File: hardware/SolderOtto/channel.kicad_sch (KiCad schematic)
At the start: 16 parts, among them J601 Conn_01x07

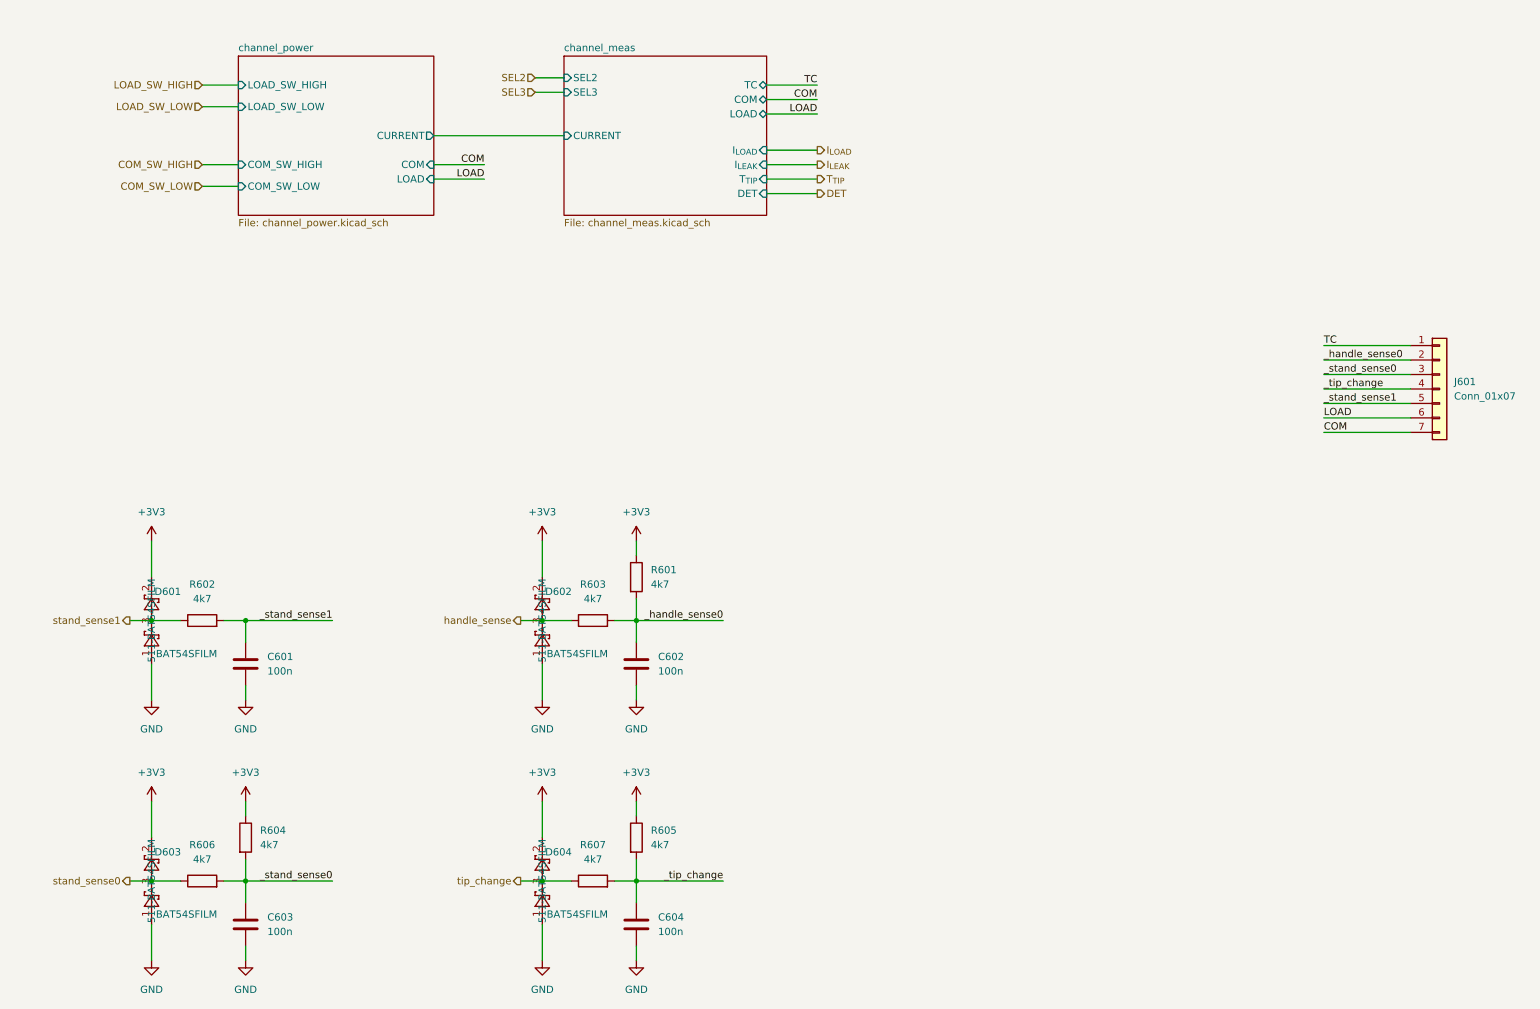
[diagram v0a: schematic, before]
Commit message: add support for tweezers AM-120
change mcu to stm32h573VI
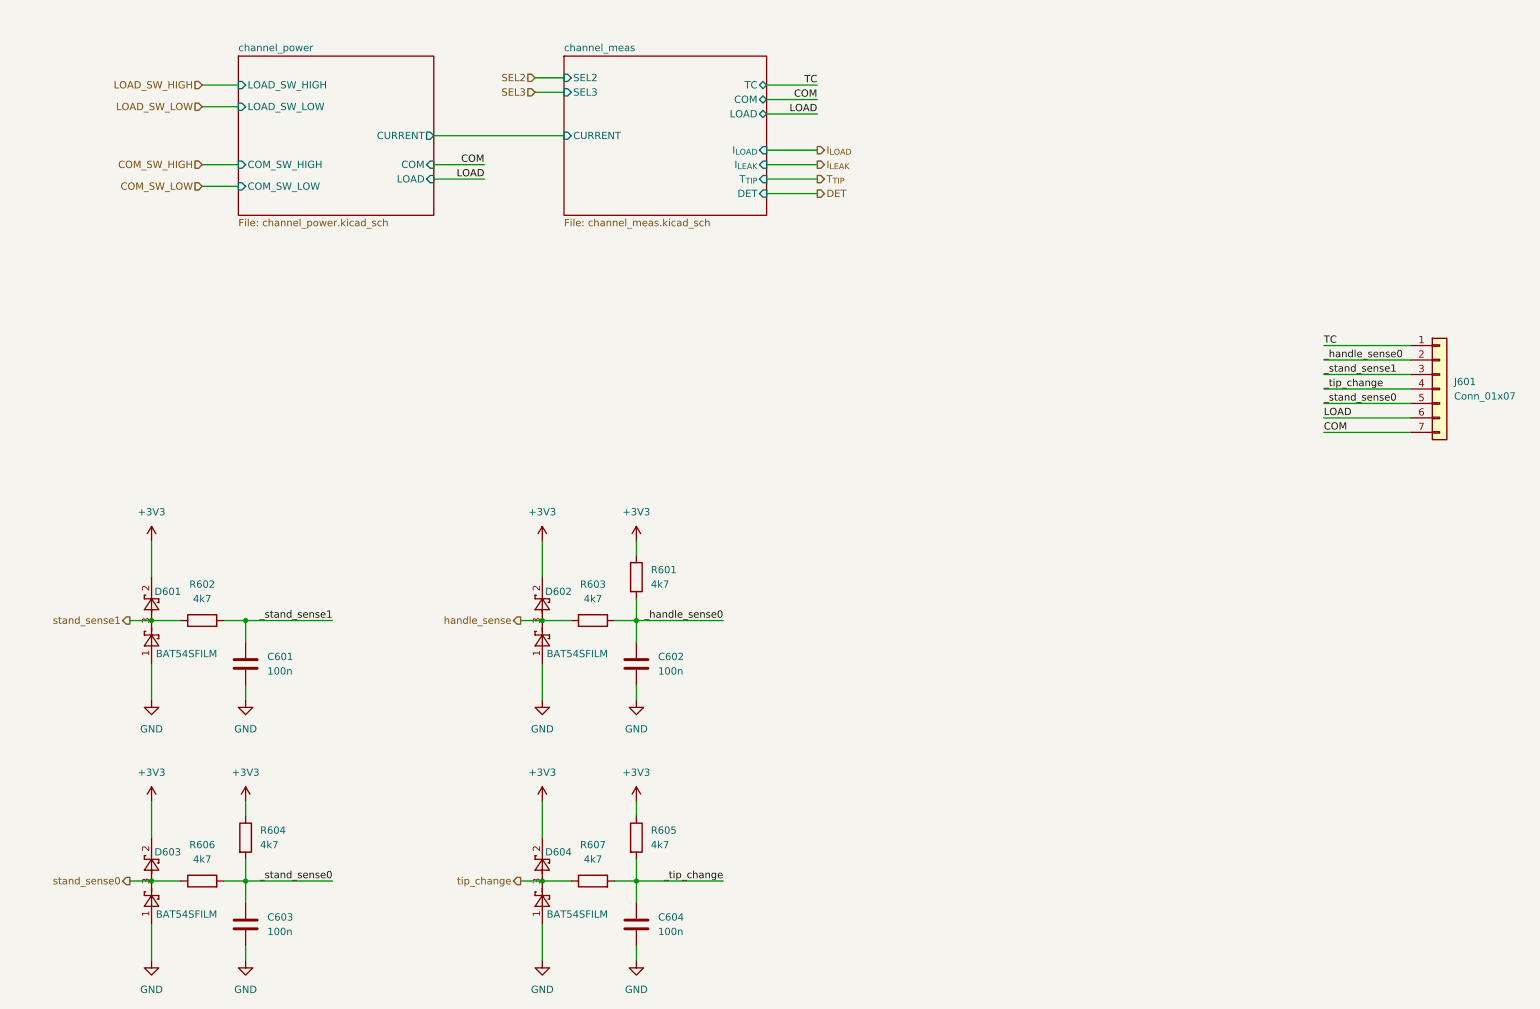
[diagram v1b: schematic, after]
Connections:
- net _stand_sense0: now also J601.5 (Pin_5); no longer J601.3 (Pin_3)
- net _stand_sense1: now also J601.3 (Pin_3); no longer J601.5 (Pin_5)
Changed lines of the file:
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@@
 	)
 	(label "_stand_sense0"
-		(at 248.92 86.36 0)
+		(at 248.92 91.44 0)
 		(fields_autoplaced yes)
 		(effects
@@
 	)
 	(label "_stand_sense1"
-		(at 248.92 91.44 0)
+		(at 248.92 86.36 0)
 		(fields_autoplaced yes)
 		(effects
@@
 	)
 	(symbol
+		(lib_name "BAT54SFILM_1")
 		(lib_id "mylib_diodes:BAT54SFILM")
 		(at 43.18 175.26 90)
@@
 					(size 1.27 1.27)
 				)
+				(hide yes)
 			)
 		)
@@
 					(size 1.27 1.27)
 				)
+				(hide yes)
 			)
 		)
@@
 					(size 1.27 1.27)
 				)
+				(hide yes)
 			)
 		)
@@
 					(size 1.27 1.27)
 				)
+				(hide yes)
 			)
 		)
@@
 			(project "SolderOtto"
 				(path "/04e99464-bf33-4a4f-8397-d26b5ec904f3/57a4c2b0-a7ab-4dc9-9bcc-6bd7e1b882d1"
-					(page "7")
+					(page "8")
 				)
 			)
@@
 			(project "SolderOtto"
 				(path "/04e99464-bf33-4a4f-8397-d26b5ec904f3/57a4c2b0-a7ab-4dc9-9bcc-6bd7e1b882d1"
-					(page "8")
-				)
-			)
+					(page "9")
+				)
+			)

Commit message: save wip
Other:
- added sheet power_latch (power_latch.kicad_sch)

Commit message: wip
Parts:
- added D605, D606: D, symbol Device:D
- added HEATER601: AM120, symbol mylib_connectors:JBC-AM120
- added HEATER602: T245, symbol mylib_connectors:JBC-T245
- added HEATER603: T210, symbol mylib_connectors:JBC-T210
- added X601, X603, X605: Binder_IP40_07, symbol mylib_connectors:Binder_IP40_07
- added X602: Binder_IP40_06, symbol mylib_connectors:Binder_IP40_06
- added X604, X606: Hirose RPC1-12RB-6P, symbol mylib_connectors:Hirose RPC1-12RB-6P
- D601: value BAT54SFILM -> BAS70S; Mouser 511-BAT54SFILM -> 3757-BAS70S_R1_00001CT-ND
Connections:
- net _handle_sense0 renamed _handle_id
- net _stand_sense0 renamed _stand_sense
- net _stand_sense1 renamed _iron_sense
- net handle_sense renamed handle_id
- net stand_sense0 renamed stand_sense
- net stand_sense1 renamed iron_sense
- new net: HEATER603.1, X605.1, X606.1
- new net: HEATER603.2, X605.6, X606.2
- new net: HEATER603.5, X605.7, X606.5
- new net: HEATER603.6, X605.2, X606.6
- new net: HEATER602.1, X603.1, X604.1
- new net: HEATER602.2, X603.6, X604.2
- new net: HEATER602.5, X603.7, X604.5
- new net: X603.2, X604.6
- new net: D605.1 (K), D606.2 (A), X601.7
- new net: D605.2 (A), HEATER601.4, X602.4
- new net: X605.3, X605.5
- new net: D606.1 (K), HEATER601.3, X602.3
- new net: HEATER601.1, X601.1, X602.1
- new net: HEATER601.2, X601.3, X602.2
- new net: HEATER601.5, X601.6, X602.5
- new net: HEATER601.6, X601.2, X602.6
- new net: X603.3, X603.5
- no-connect marks 0 -> 6
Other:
- sheet channel_meas ports: added LOAD0, LOAD1, SEL1; removed LOAD
- sheet channel_power ports: added LOAD0, LOAD0_SW_HIGH, LOAD1, LOAD1_SW_HIGH; removed LOAD, LOAD_SW_HIGH
- sheet power_latch ports: added COM_SW, IN_LOAD0_H, IN_LOAD1_H, OUT_LOAD0_H, OUT_LOAD1_H; removed IN_COM_L, IN_LOAD_H, IN_LOAD_L, OUT_LOAD_H
- note added: "AM-AD-SF"
- note added: "AM-SB"
- moved on the sheet: C601, C602, C603, C604, D601, D602, D603, D604, J601, R601, R602, R603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

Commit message: save wip
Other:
- sheet power_latch ports: added LOW_SIDE_SW; removed COM_SW

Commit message: update schematic
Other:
- sheet power_latch ports: added IN_COM, IN_LOAD0, IN_LOAD1, LOW_SIDE; removed IN_COM_H, IN_LOAD0_H, IN_LOAD1_H, LOW_SIDE_SW

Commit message: fix electrical findings
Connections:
- no-connect marks 6 -> 8
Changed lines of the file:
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@@
 	)
 	(no_connect
+		(at 35.56 87.63)
+	)
+	(no_connect
+		(at 38.1 83.82)
+	)
+	(no_connect
 		(at 58.42 121.92)
 	)
@@
 	)
 	(symbol
+		(lib_id "mylib_connectors:JBC-AM120")
+		(at 100.33 86.36 0)
+		(unit 1)
+		(exclude_from_sim yes)
+		(in_bom no)
+		(on_board no)
+		(dnp no)
+		(fields_autoplaced yes)
+		(property "Reference" "HEATER601"
+			(at 111.76 85.4074 0)
+			(effects
+				(font
+					(size 1.27 1.27)
+				)
+				(justify left)
+			)
+		)
+		(property "Value" "AM120"
+			(at 111.76 87.9474 0)
+			(effects
+				(font
+					(size 1.27 1.27)
+				)
+				(justify left)
+			)
+		)
+		(property "Footprint" ""
+			(at 49.53 87.63 0)
+			(effects
+				(font
+					(size 1.27 1.27)
+				)
+				(hide yes)
+			)
+		)
+		(property "Datasheet" ""
+			(at 49.53 87.63 0)
+			(effects
+				(font
+					(size 1.27 1.27)
+				)
+				(hide yes)
+			)
+		)
+		(property "Description" ""
+			(at 49.53 87.63 0)
+			(effects
+				(font
+					(size 1.27 1.27)
+				)
+				(hide yes)
+			)
+		)
+		(pin "2"
+		)
+		(pin "3"
+		)
+		(pin "4"
+		)
+		(pin "5"
+		)
+		(pin "1"
+		)
+		(pin "1"
+		)
+		(pin "6"
+		)
+		(instances
+			(project ""
+				(path "/04e99464-bf33-4a4f-8397-d26b5ec904f3/57a4c2b0-a7ab-4dc9-9bcc-6bd7e1b882d1"
+					(reference "HEATER601")
+					(unit 1)
+				)
+			)
+		)
+	)
+	(symbol
 		(lib_id "mylib_connectors:Hirose RPC1-12RB-6P")
 		(at 62.23 157.48 90)
@@
 					(unit 1)
 				)
-			)
-		)
-	)
-	(symbol
-		(lib_id "mylib_connectors:JBC-AM120")
-		(at 100.33 86.36 0)
-		(unit 1)
-		(exclude_from_sim yes)
-		(in_bom no)
-		(on_board no)
-		(dnp no)
-		(property "Reference" "HEATER601"
-			(at 111.76 85.4074 0)
-			(effects
-				(font
-					(size 1.27 1.27)
-				)
-				(justify left)
-				(hide yes)
-			)
-		)
-		(property "Value" "AM120"
-			(at 97.028 71.12 0)
-			(effects
-				(font
-					(size 1.27 1.27)
-				)
-				(justify left)
-			)
-		)
-		(property "Footprint" ""
-			(at 49.53 87.63 0)
-			(effects
-				(font
-					(size 1.27 1.27)
-				)
-				(hide yes)
-			)
-		)
-		(property "Datasheet" ""
-			(at 49.53 87.63 0)
-			(effects
-				(font
-					(size 1.27 1.27)
-				)
-				(hide yes)
-			)
-		)
-		(property "Description" ""
-			(at 49.53 87.63 0)
-			(effects
-				(font
-					(size 1.27 1.27)
-				)
-				(hide yes)
-			)
-		)
-		(pin "2"
-		)
-		(pin "1"
-		)
-		(pin "1"
-		)
-		(pin "3"
-		)
-		(pin "4"
-		)
-		(pin "5"
-		)
-		(pin "6"
-		)
-		(instances
-			(project "SolderOtto"
-				(path "/04e99464-bf33-4a4f-8397-d26b5ec904f3/57a4c2b0-a7ab-4dc9-9bcc-6bd7e1b882d1"
-					(reference "HEATER601")
-					(unit 1)
-				)

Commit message: create adapter to enclosure for display
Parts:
- renumbered D605 to D601, D606 to D602, D601 to D603, D602 to D604, D603 to D605, D604 to D606
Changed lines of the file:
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@@
 		(on_board yes)
 		(dnp no)
-		(property "Reference" "D603"
+		(property "Reference" "D605"
 			(at 191.008 130.81 90)
 			(effects
@@
 			(project "SolderOtto"
 				(path "/04e99464-bf33-4a4f-8397-d26b5ec904f3/57a4c2b0-a7ab-4dc9-9bcc-6bd7e1b882d1"
-					(reference "D603")
+					(reference "D605")
 					(unit 1)
 				)
@@
 		(dnp no)
 		(fields_autoplaced yes)
-		(property "Reference" "D605"
+		(property "Reference" "D601"
 			(at 52.07 83.82 0)
 			(effects
@@
 			(project "SolderOtto"
 				(path "/04e99464-bf33-4a4f-8397-d26b5ec904f3/57a4c2b0-a7ab-4dc9-9bcc-6bd7e1b882d1"
-					(reference "D605")
+					(reference "D601")
 					(unit 1)
 				)
@@
 		(on_board yes)
 		(dnp no)
-		(property "Reference" "D604"
+		(property "Reference" "D606"
 			(at 246.888 130.81 90)
 			(effects
@@
 			(project "SolderOtto"
 				(path "/04e99464-bf33-4a4f-8397-d26b5ec904f3/57a4c2b0-a7ab-4dc9-9bcc-6bd7e1b882d1"
-					(reference "D604")
+					(reference "D606")
 					(unit 1)
 				)
@@
 		(dnp no)
 		(fields_autoplaced yes)
-		(property "Reference" "D606"
+		(property "Reference" "D602"
 			(at 52.07 74.93 0)
 			(effects
@@
 			(project "SolderOtto"
 				(path "/04e99464-bf33-4a4f-8397-d26b5ec904f3/57a4c2b0-a7ab-4dc9-9bcc-6bd7e1b882d1"
-					(reference "D606")
+					(reference "D602")
 					(unit 1)
 				)
@@
 		(on_board yes)
 		(dnp no)
-		(property "Reference" "D602"
+		(property "Reference" "D604"
 			(at 246.888 85.09 90)
 			(effects
@@
 			(project "SolderOtto"
 				(path "/04e99464-bf33-4a4f-8397-d26b5ec904f3/57a4c2b0-a7ab-4dc9-9bcc-6bd7e1b882d1"
-					(reference "D602")
+					(reference "D604")
 					(unit 1)
 				)
@@
 		(on_board yes)
 		(dnp no)
-		(property "Reference" "D601"
+		(property "Reference" "D603"
 			(at 191.008 85.09 90)
 			(effects
@@
 			(project "SolderOtto"
 				(path "/04e99464-bf33-4a4f-8397-d26b5ec904f3/57a4c2b0-a7ab-4dc9-9bcc-6bd7e1b882d1"
-					(reference "D601")
+					(reference "D603")
 					(unit 1)
 				)
@@
 			(project "SolderOtto"
 				(path "/04e99464-bf33-4a4f-8397-d26b5ec904f3/57a4c2b0-a7ab-4dc9-9bcc-6bd7e1b882d1"
-					(page "8")
+					(page "9")
 				)
 			)
@@
 			(project "SolderOtto"
 				(path "/04e99464-bf33-4a4f-8397-d26b5ec904f3/57a4c2b0-a7ab-4dc9-9bcc-6bd7e1b882d1"
-					(page "9")
-				)
-			)
+					(page "8")
+				)
+			)

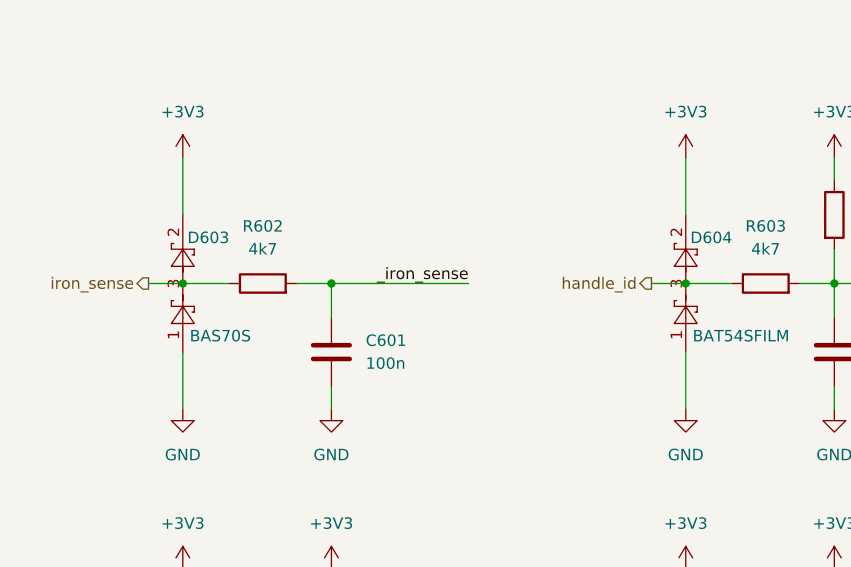
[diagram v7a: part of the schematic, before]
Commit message: try to replace op07c
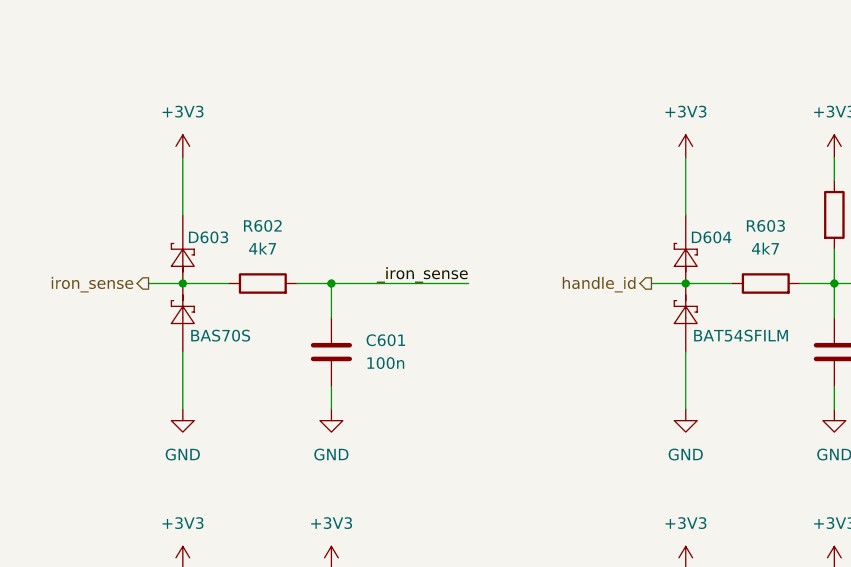
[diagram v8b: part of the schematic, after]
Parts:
- D603: Mouser 3757-BAS70S_R1_00001CT-ND -> 511-BAT54SFILM
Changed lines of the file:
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@@
 	)
 	(symbol
-		(lib_name "BAT54SFILM_1")
 		(lib_id "mylib_diodes:BAT54SFILM")
 		(at 190.5 135.89 90)
@@
 	)
 	(symbol
-		(lib_name "BAT54SFILM_2")
 		(lib_id "mylib_diodes:BAT54SFILM")
 		(at 246.38 135.89 90)
@@
 			)
 		)
-		(property "Mouser" "3757-BAS70S_R1_00001CT-ND"
+		(property "Mouser" "511-BAT54SFILM"
 			(at 190.5 90.17 0)
 			(effects
